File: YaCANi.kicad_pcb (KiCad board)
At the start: 2 copper layers, 26 parts, among them P1 SWD, P2 CAN, P3 USB, U1 STM32F042C6T6, U2 MCP2562-E/SN, U3 LD1117S33TR

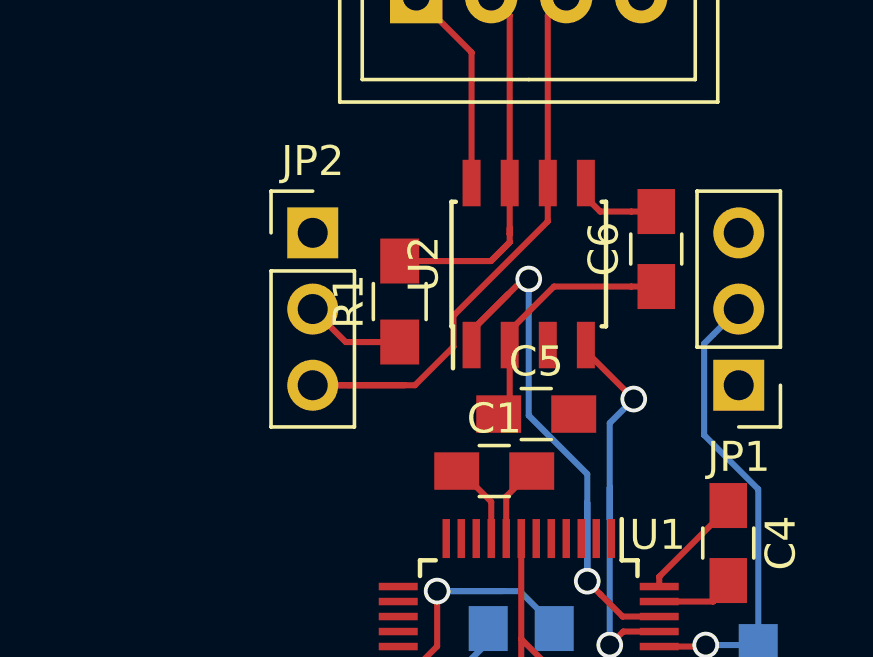
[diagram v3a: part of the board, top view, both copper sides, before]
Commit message: just change a via
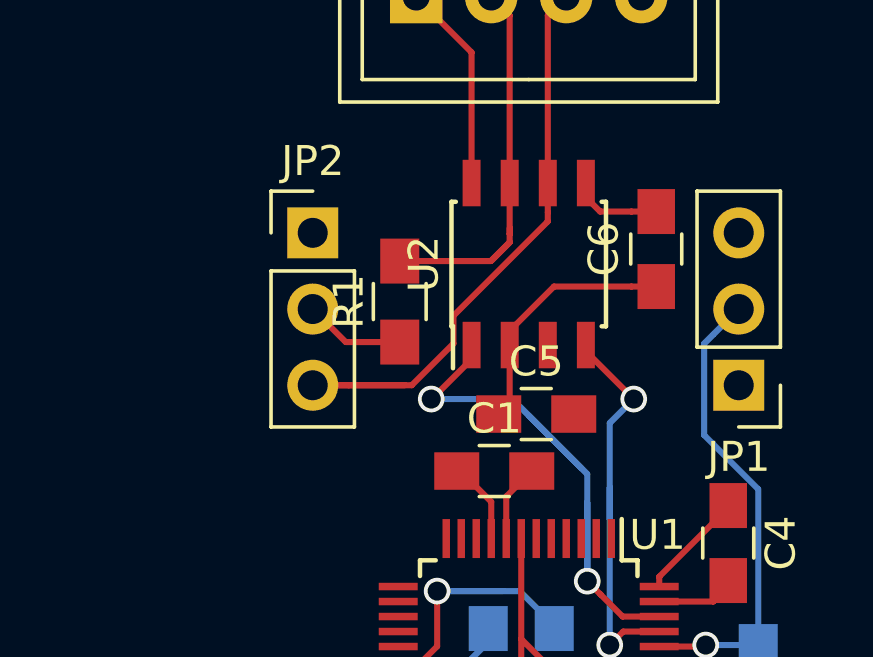
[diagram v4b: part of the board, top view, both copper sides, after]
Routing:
- net /CAN_TX: track 21.2 -> 20.2 mm
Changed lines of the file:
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@@
   (general
     (links 67)
-    (no_connects 46)
-    (area 0 0 0 0)
+    (no_connects 31)
+    (area 79.892857 69.8 154.6 144.625)
     (thickness 1.6)
     (drawings 6)
-    (tracks 171)
+    (tracks 172)
     (zones 0)
     (modules 26)
@@
   (segment (start 134.9 102.75) (end 134.45 103.2) (width 0.2032) (layer F.Cu) (net 7))
   (via (at 134.45 103.2) (size 0.889) (drill 0.635) (layers F.Cu B.Cu) (net 7))
+  (segment (start 131.75 95.54931) (end 133.5 97.29931) (width 0.2032) (layer B.Cu) (net 8))
+  (segment (start 133.5 97.29931) (end 133.70069 97.5) (width 0.2032) (layer B.Cu) (net 8))
+  (segment (start 128.5 95) (end 131.20069 95) (width 0.2032) (layer B.Cu) (net 8))
+  (segment (start 131.20069 95) (end 133.5 97.29931) (width 0.2032) (layer B.Cu) (net 8))
+  (via (at 128.5 95) (size 0.889) (drill 0.635) (layers F.Cu B.Cu) (net 8))
+  (segment (start 129.845 93.2) (end 129.845 93.675) (width 0.2032) (layer F.Cu) (net 8))
+  (segment (start 129.845 93.675) (end 128.52 95) (width 0.2032) (layer F.Cu) (net 8))
+  (segment (start 128.52 95) (end 128.5 95) (width 0.2032) (layer F.Cu) (net 8))
   (segment (start 133.70069 101.07064) (end 133.70069 97.5) (width 0.2032) (layer B.Cu) (net 8))
-  (segment (start 131.75 91) (end 131.75 95.54931) (width 0.2032) (layer B.Cu) (net 8))
-  (segment (start 131.75 95.54931) (end 133.70069 97.5) (width 0.2032) (layer B.Cu) (net 8))
-  (segment (start 129.845 93.2) (end 129.845 92.725) (width 0.2032) (layer F.Cu) (net 8))
-  (segment (start 129.845 92.725) (end 131.57 91) (width 0.2032) (layer F.Cu) (net 8))
-  (segment (start 131.57 91) (end 131.75 91) (width 0.2032) (layer F.Cu) (net 8))
-  (segment (start 131.07 91.5) (end 129.845 92.725) (width 0.2032) (layer F.Cu) (net 8))
-  (via (at 131.75 91) (size 0.889) (drill 0.635) (layers F.Cu B.Cu) (net 8))
   (segment (start 133.70069 99.4) (end 133.70069 101.07064) (width 0.2032) (layer B.Cu) (net 8))
   (segment (start 133.70069 98.45069) (end 133.70069 99.4) (width 0.2032) (layer B.Cu) (net 8))
@@
   (segment (start 137.6 103.25) (end 137.65 103.2) (width 0.2032) (layer F.Cu) (net 15))
   (via (at 137.65 103.2) (size 0.889) (drill 0.635) (layers F.Cu B.Cu) (net 15))
-  (segment (start 129.240199 92.181159) (end 129.283591 92.181159) (width 0.2032) (layer F.Cu) (net 16))
-  (segment (start 129.283591 92.181159) (end 132.385 89.07975) (width 0.2032) (layer F.Cu) (net 16))
-  (segment (start 124.55 94.54) (end 127.958642 94.54) (width 0.2032) (layer F.Cu) (net 16))
-  (segment (start 127.958642 94.54) (end 129.240199 93.258443) (width 0.2032) (layer F.Cu) (net 16))
-  (segment (start 129.240199 93.258443) (end 129.240199 92.181159) (width 0.2032) (layer F.Cu) (net 16))
-  (segment (start 132.385 89.07975) (end 132.385 87.8) (width 0.2032) (layer F.Cu) (net 16))
+  (segment (start 132.385 88.7782) (end 132.385 87.8) (width 0.2032) (layer F.Cu) (net 16))
+  (segment (start 132.385 89.07975) (end 132.385 88.7782) (width 0.2032) (layer F.Cu) (net 16))
+  (segment (start 129.240199 92.224551) (end 132.385 89.07975) (width 0.2032) (layer F.Cu) (net 16))
+  (segment (start 129.240199 93.150833) (end 129.240199 92.224551) (width 0.2032) (layer F.Cu) (net 16))
+  (segment (start 127.851032 94.54) (end 129.240199 93.150833) (width 0.2032) (layer F.Cu) (net 16))
+  (segment (start 124.55 94.54) (end 127.851032 94.54) (width 0.2032) (layer F.Cu) (net 16))
   (segment (start 132.385 87.8) (end 132.385 82.215) (width 0.2032) (layer F.Cu) (net 16))
   (segment (start 132.385 82.215) (end 133 81.6) (width 0.2032) (layer F.Cu) (net 16))

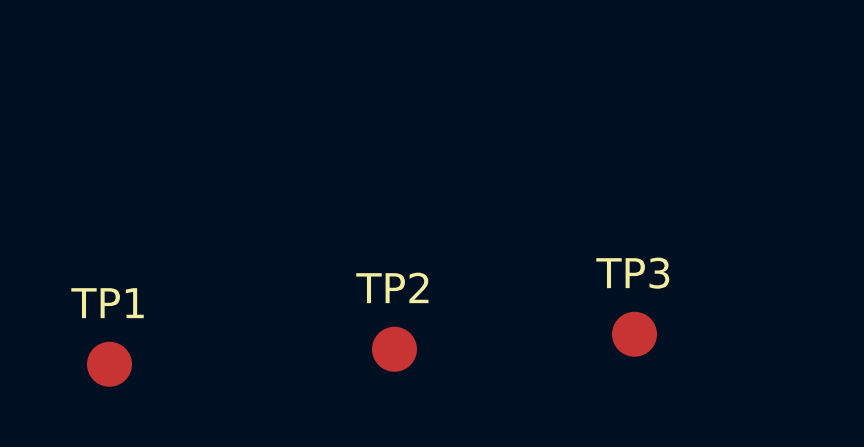
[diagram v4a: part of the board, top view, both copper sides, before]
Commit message: remove test points
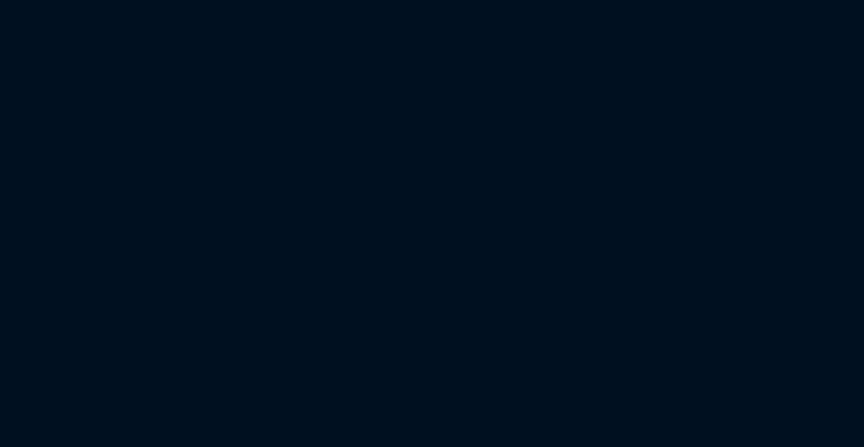
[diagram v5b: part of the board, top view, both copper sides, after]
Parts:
- removed TP1: 5V, Measurement_Points:Measurement_Point_Round-SMD-Pad_Small
- removed TP2: CAN_Rx, Measurement_Points:Measurement_Point_Round-SMD-Pad_Small
- removed TP3: CAN_Tx, Measurement_Points:Measurement_Point_Round-SMD-Pad_Small
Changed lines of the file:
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@@
 (kicad_pcb (version 4) (host pcbnew 4.0.6)
   (general
-    (links 67)
-    (no_connects 31)
-    (area 79.892857 69.8 154.6 144.625)
+    (links 64)
+    (no_connects 28)
+    (area 0 0 0 0)
     (thickness 1.6)
     (drawings 6)
     (tracks 172)
     (zones 0)
-    (modules 26)
+    (modules 23)
     (nets 20)
   )
@@
     )
   )
-  (module Measurement_Points:Measurement_Point_Round-SMD-Pad_Small (layer F.Cu)
-    (at 81.75 141.25)
-    (descr "Mesurement Point, Round, SMD Pad, DM 1.5mm,")
-    (tags "Mesurement Point Round SMD Pad 1.5mm")
-    (attr virtual)
-    (fp_text reference TP1 (at 0 -2) (layer F.SilkS)
-      (effects (font (size 1 1) (thickness 0.15)))
-    )
-    (fp_text value 5V (at 0 2) (layer F.Fab)
-      (effects (font (size 1 1) (thickness 0.15)))
-    )
-    (fp_circle (center 0 0) (end 1 0) (layer F.CrtYd) (width 0.05))
-    (pad 1 smd circle (at 0 0) (size 1.5 1.5) (layers F.Cu F.Mask)
-      (net 2 +5V))
-  )
-  (module Measurement_Points:Measurement_Point_Round-SMD-Pad_Small (layer F.Cu)
-    (at 91.25 140.75)
-    (descr "Mesurement Point, Round, SMD Pad, DM 1.5mm,")
-    (tags "Mesurement Point Round SMD Pad 1.5mm")
-    (attr virtual)
-    (fp_text reference TP2 (at 0 -2) (layer F.SilkS)
-      (effects (font (size 1 1) (thickness 0.15)))
-    )
-    (fp_text value CAN_Rx (at 0 2) (layer F.Fab)
-      (effects (font (size 1 1) (thickness 0.15)))
-    )
-    (fp_circle (center 0 0) (end 1 0) (layer F.CrtYd) (width 0.05))
-    (pad 1 smd circle (at 0 0) (size 1.5 1.5) (layers F.Cu F.Mask)
-      (net 7 /CAN_RX))
-  )
-  (module Measurement_Points:Measurement_Point_Round-SMD-Pad_Small (layer F.Cu)
-    (at 99.25 140.25)
-    (descr "Mesurement Point, Round, SMD Pad, DM 1.5mm,")
-    (tags "Mesurement Point Round SMD Pad 1.5mm")
-    (attr virtual)
-    (fp_text reference TP3 (at 0 -2) (layer F.SilkS)
-      (effects (font (size 1 1) (thickness 0.15)))
-    )
-    (fp_text value CAN_Tx (at 0 2) (layer F.Fab)
-      (effects (font (size 1 1) (thickness 0.15)))
-    )
-    (fp_circle (center 0 0) (end 1 0) (layer F.CrtYd) (width 0.05))
-    (pad 1 smd circle (at 0 0) (size 1.5 1.5) (layers F.Cu F.Mask)
-      (net 8 /CAN_TX))
-  )
   (module Pin_Headers:Pin_Header_Straight_1x05_Pitch2.54mm (layer F.Cu)

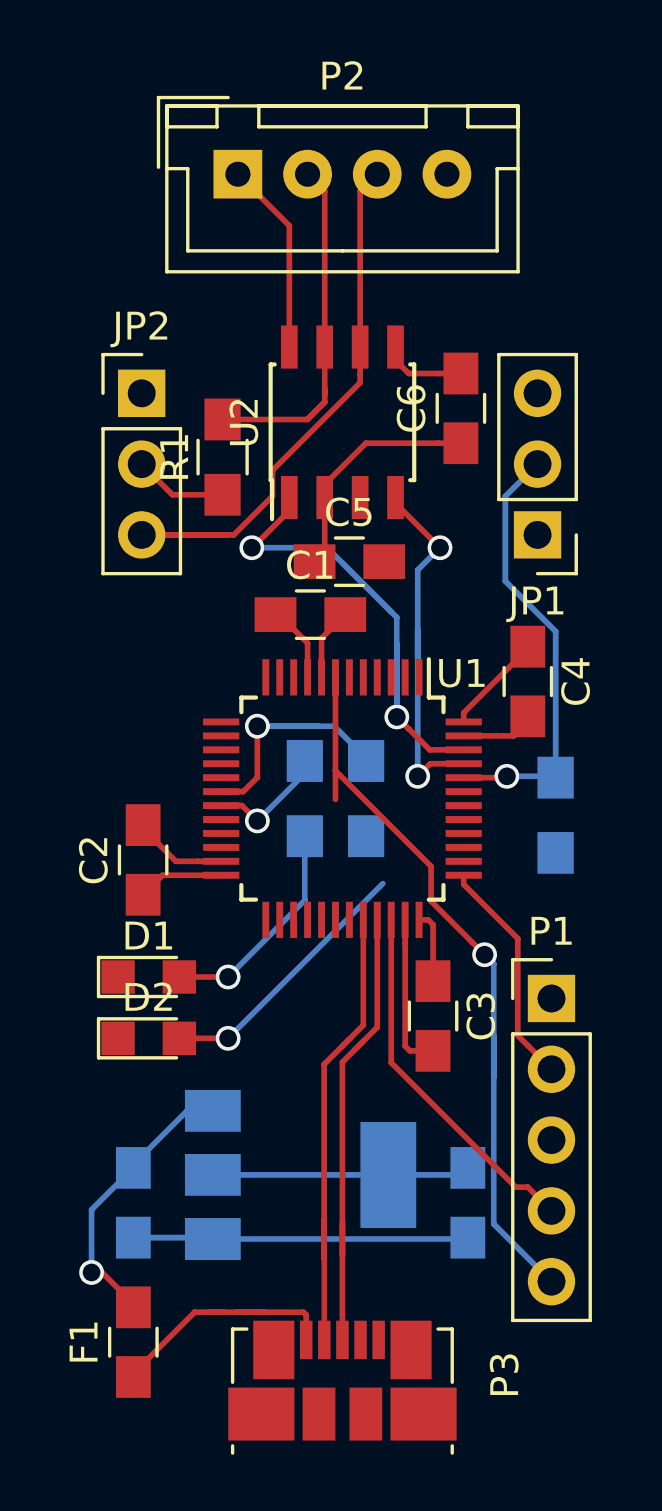
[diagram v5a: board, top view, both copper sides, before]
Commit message: proper track size
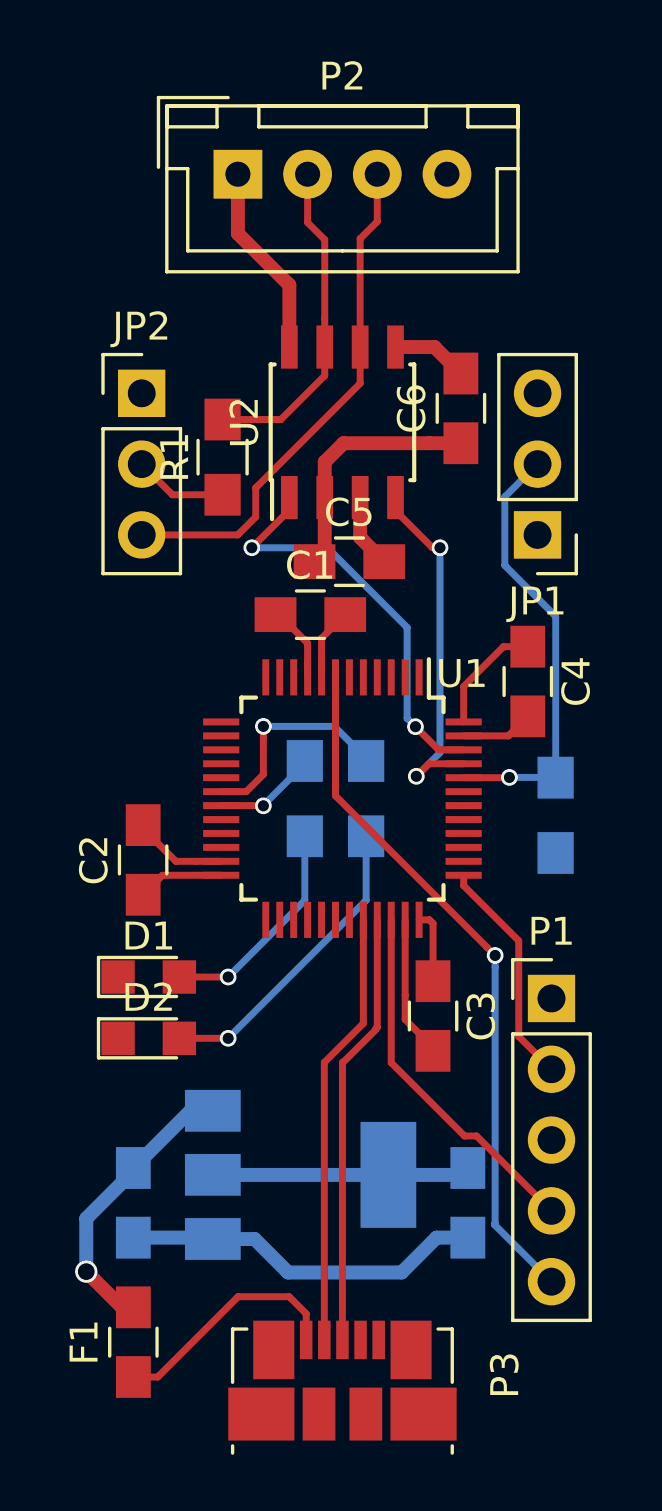
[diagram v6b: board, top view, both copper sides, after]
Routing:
- net /USB_DP: track 17.2 -> 23.8 mm
- net /CAN_TX: track 20.2 -> 14.9 mm
- net CAN_L: track 21.4 -> 18.5 mm
- net +5V: track 10.2 -> 13.1 mm
- net /NRST: track 27.4 -> 24.9 mm
- net LED_PWR: track 10.0 -> 7.75 mm
- net /USB_DM: track 17.4 -> 15.6 mm
- net CAN_H: track 13.4 -> 11.8 mm
- net Net-(D2-Pad2): track 9.60 -> 11.1 mm
- net Net-(F1-Pad1): track 9.77 -> 8.59 mm
- net GND: track 41.5 -> 42.7 mm
- net /CAN_RX: track 13.9 -> 13.1 mm
- net LED_ACT: track 4.38 -> 3.74 mm
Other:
- net class DRC added: clearance 0.65, trace_width 0.5, via_dia 0.6, via_drill 0.4
- net class Default: clearance 0.2032 -> 0.2; trace_width 0.2032 -> 0.25; via_dia 0.889 -> 0.6; via_drill 0.635 -> 0.4
- net class Interm added: clearance 0.4, trace_width 0.5, via_dia 0.8, via_drill 0.6
- net class Mounting Hole removed
- net class PWR added: clearance 0.8, trace_width 1.5, via_dia 0.6, via_drill 0.4
- net class Signal added: clearance 0.2, trace_width 0.25, via_dia 0.6, via_drill 0.4
- rule trace_clearance: 0.2032 -> 0.2
- rule trace_min: 0.2032 -> 0.2
- rule via_min_drill: 0.508 -> 0.3
- rule via_min_size: 0.889 -> 0.4

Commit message: DRC ok
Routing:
- net +3V3: track 24.7 -> 108.2 mm, vias 0 -> 6
- net GND: track 42.7 -> 110.9 mm, vias 0 -> 4
- net +5V: track 13.1 -> 45.2 mm, vias 1 -> 3
- net /SWDIO: track 13.1 -> 15.8 mm
- net /CAN_TX: track 14.9 -> 16.4 mm
- net /CAN_RX: track 13.1 -> 12.0 mm, vias 2 -> 0
- net /NRST: track 24.9 -> 26.0 mm
- net /SWCLK: track 8.26 -> 8.94 mm
- added copper zone on B.Cu, net GND
- added copper zone on F.Cu, net GND
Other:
- board outline added: 20 x 50 mm

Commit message: first version ?
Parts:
- added REF**: Via, PhoenixRobotik:Via-0.6mm, F.Cu at (139.2, 125.0)
- added REF**: Via, PhoenixRobotik:Via-0.6mm, F.Cu at (124.2, 100.0)
- added REF**: Via, PhoenixRobotik:Via-0.6mm, F.Cu at (134.2, 90.0)
- added REF**: Via, PhoenixRobotik:Via-0.6mm, F.Cu at (139.2, 87.5)
- added REF**: Via, PhoenixRobotik:Via-0.6mm, F.Cu at (126.8, 87.5)
- added REF**: Via, PhoenixRobotik:Via-0.6mm, F.Cu at (124.2, 87.5)
- added REF**: Via, PhoenixRobotik:Via-0.6mm, F.Cu at (139.2, 85.0)
- added REF**: Via, PhoenixRobotik:Via-0.6mm, F.Cu at (136.8, 85.0)
- added REF**: Via, PhoenixRobotik:Via-0.6mm, F.Cu at (134.2, 85.0)
- added REF**: Via, PhoenixRobotik:Via-0.6mm, F.Cu at (131.8, 85.0)
- added REF**: Via, PhoenixRobotik:Via-0.6mm, F.Cu at (129.2, 85.0)
- added REF**: Via, PhoenixRobotik:Via-0.6mm, F.Cu at (136.8, 125.0)
- added REF**: Via, PhoenixRobotik:Via-0.6mm, F.Cu at (126.8, 85.0)
- added REF**: Via, PhoenixRobotik:Via-0.6mm, F.Cu at (124.2, 85.0)
- added REF**: Via, PhoenixRobotik:Via-0.6mm, F.Cu at (139.2, 82.5)
- added REF**: Via, PhoenixRobotik:Via-0.6mm, F.Cu at (136.8, 82.5)
- added REF**: Via, PhoenixRobotik:Via-0.6mm, F.Cu at (134.2, 82.5)
- added REF**: Via, PhoenixRobotik:Via-0.6mm, F.Cu at (131.8, 82.5)
- added REF**: Via, PhoenixRobotik:Via-0.6mm, F.Cu at (124.2, 82.5)
- added REF**: Via, PhoenixRobotik:Via-0.6mm, F.Cu at (139.2, 80.0)
- added REF**: Via, PhoenixRobotik:Via-0.6mm, F.Cu at (136.8, 80.0)
- added REF**: Via, PhoenixRobotik:Via-0.6mm, F.Cu at (134.2, 80.0)
- added REF**: Via, PhoenixRobotik:Via-0.6mm, F.Cu at (126.8, 125.0)
- added REF**: Via, PhoenixRobotik:Via-0.6mm, F.Cu at (131.8, 80.0)
- added REF**: Via, PhoenixRobotik:Via-0.6mm, F.Cu at (129.2, 80.0)
- added REF**: Via, PhoenixRobotik:Via-0.6mm, F.Cu at (126.8, 80.0)
- added REF**: Via, PhoenixRobotik:Via-0.6mm, F.Cu at (124.2, 80.0)
- added REF**: Via, PhoenixRobotik:Via-0.6mm, F.Cu at (127.5, 100.0)
- added REF**: Via, PhoenixRobotik:Via-0.6mm, F.Cu at (132.8, 101.2)
- added REF**: Via, PhoenixRobotik:Via-0.6mm, F.Cu at (128.0, 107.8)
- added REF**: Via, PhoenixRobotik:Via-0.6mm, F.Cu at (129.2, 119.8)
- added REF**: Via, PhoenixRobotik:Via-0.6mm, F.Cu at (133.2, 114.2)
- added REF**: Via, PhoenixRobotik:Via-0.6mm, F.Cu at (128.8, 106.2)
- added REF**: Via, PhoenixRobotik:Via-0.6mm, F.Cu at (136.8, 122.5)
- added REF**: Via, PhoenixRobotik:Via-0.6mm, F.Cu at (130.2, 101.0)
- added REF**: Via, PhoenixRobotik:Via-0.6mm, F.Cu at (137.8, 105.2)
- added REF**: Via, PhoenixRobotik:Via-0.6mm, F.Cu at (126.8, 95.8)
- added REF**: Via, PhoenixRobotik:Via-0.6mm, F.Cu at (129.2, 115.0)
- added REF**: Via, PhoenixRobotik:Via-0.6mm, F.Cu at (130.8, 111.0)
- added REF**: Via, PhoenixRobotik:Via-0.6mm, F.Cu at (139.2, 107.5)
- added REF**: Via, PhoenixRobotik:Via-0.6mm, F.Cu at (134.2, 104.2)
- added REF**: Via, PhoenixRobotik:Via-0.6mm, F.Cu at (124.2, 102.5)
- moved R3 0.50 mm to (130.4, 104.5)
- moved R4 0.50 mm to (132.6, 104.5)
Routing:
- net GND: track 110.9 -> 108.3 mm
- net +3V3: track 108.2 -> 107.1 mm
